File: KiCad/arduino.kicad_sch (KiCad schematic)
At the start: 15 parts, among them T3 ADS1115, T4 ADS1115

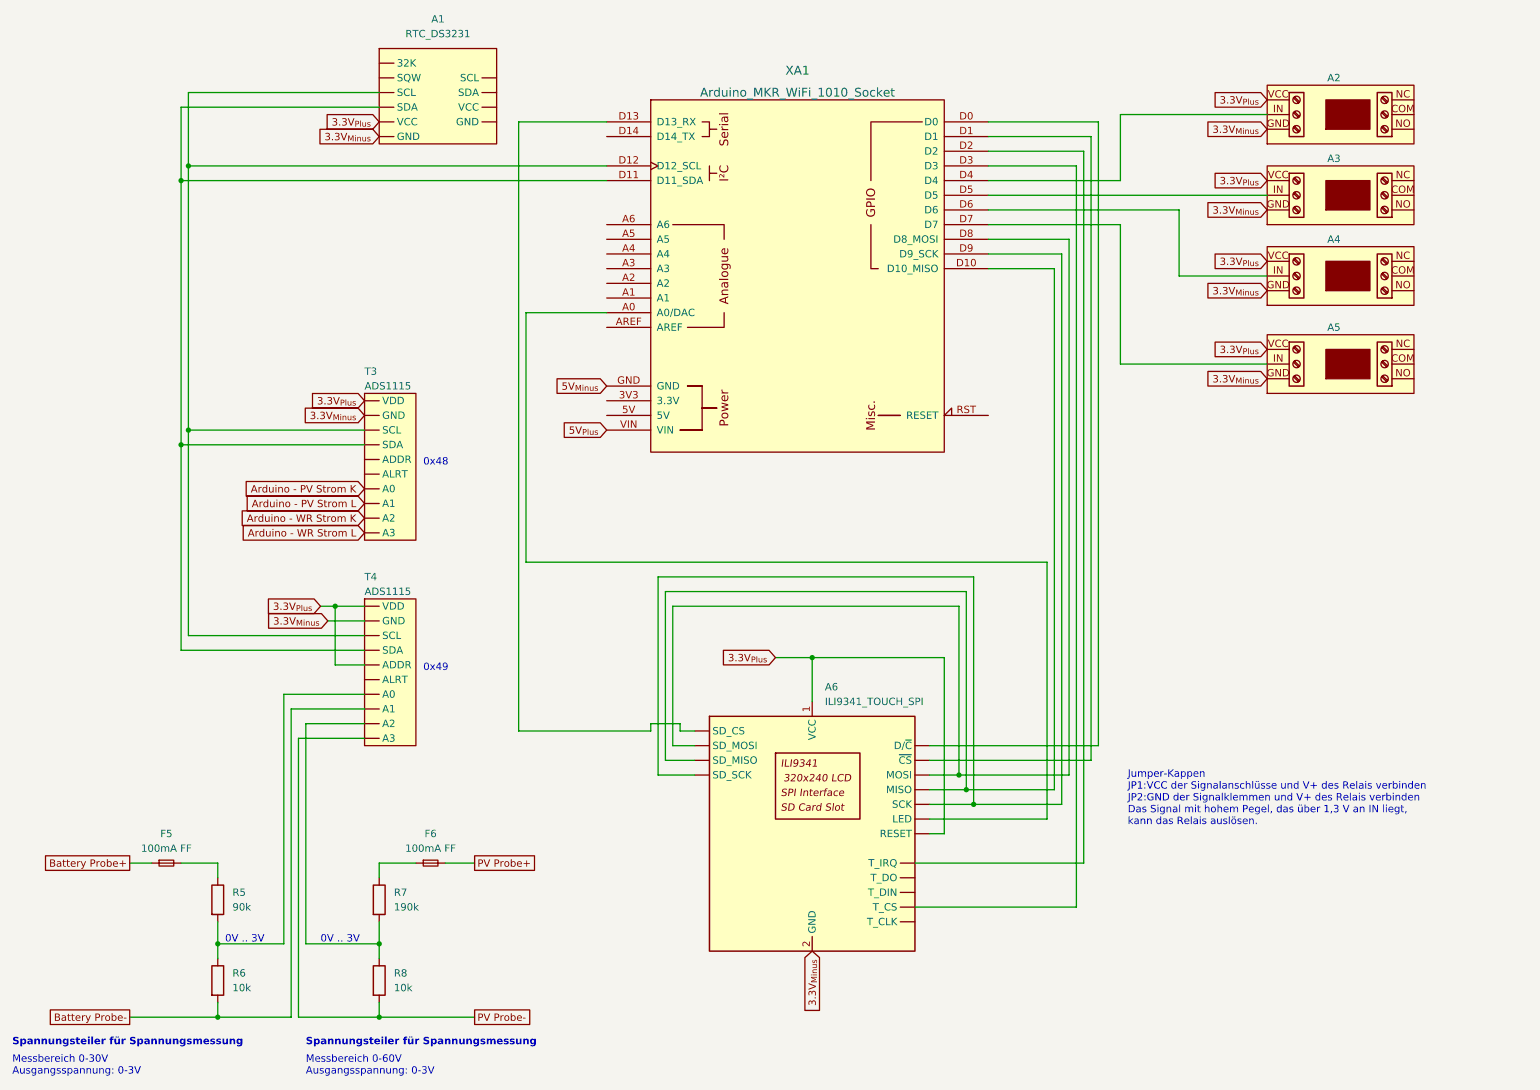
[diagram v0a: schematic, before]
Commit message: repository clean up | circuit diagram modified -> still have to add the wiring of the power supply in the circuit cabinet and the wiring of the UPS module
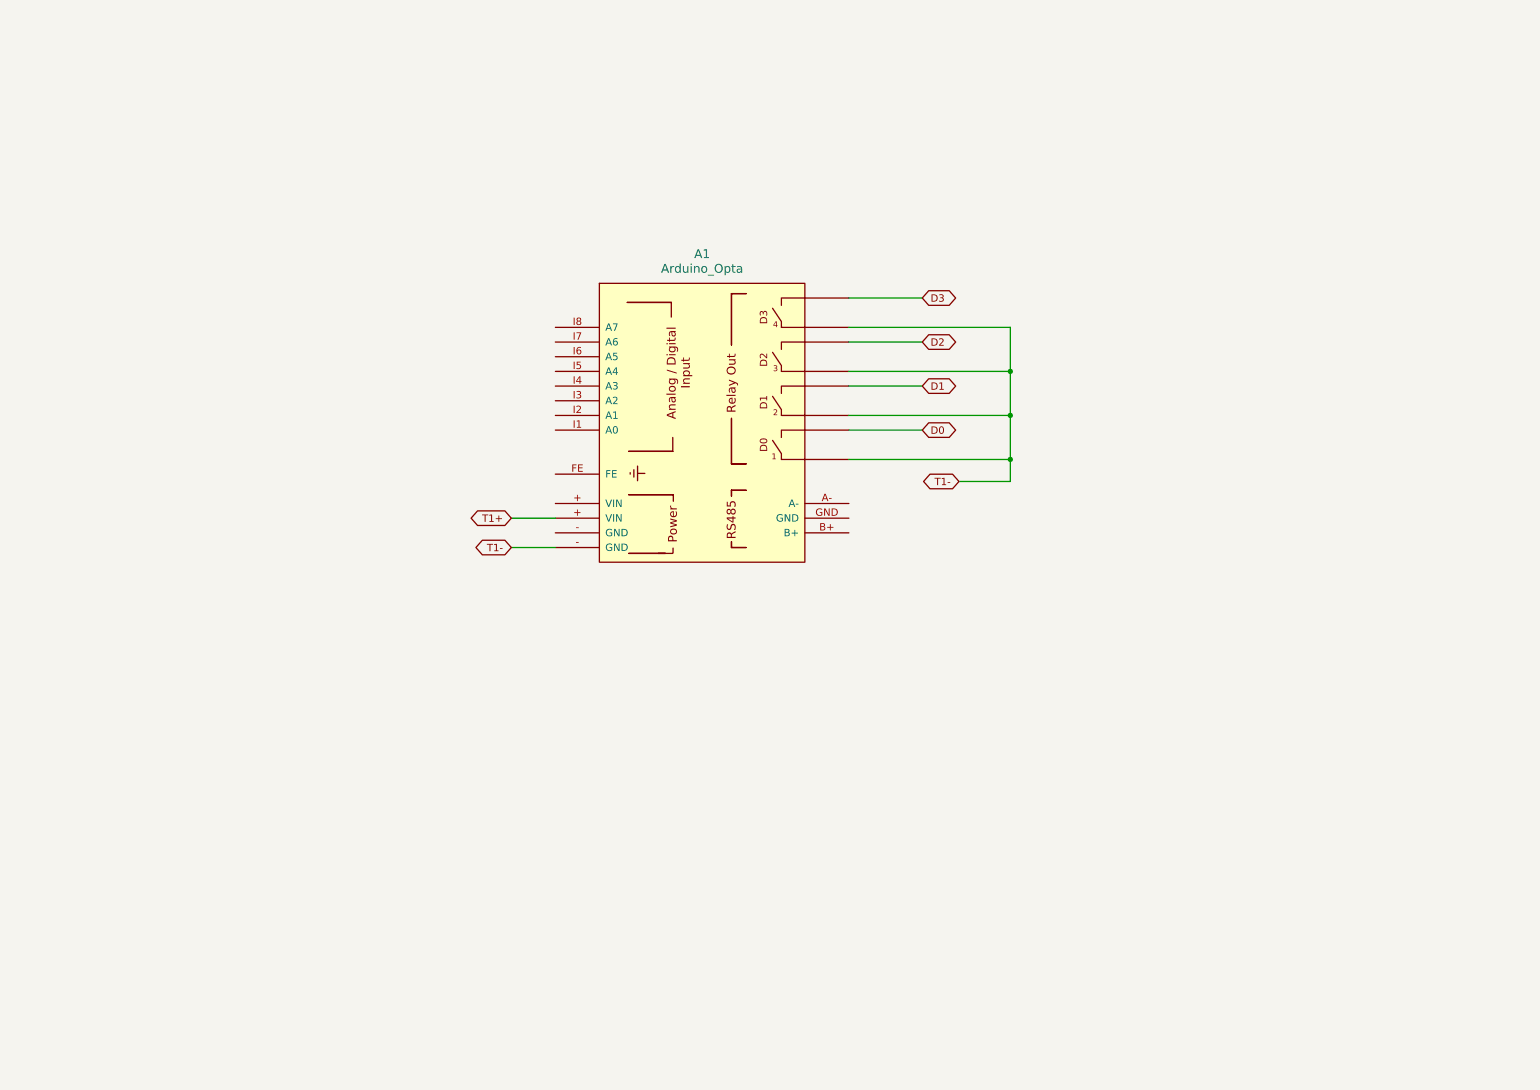
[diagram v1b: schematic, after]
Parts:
- removed A1: RTC_DS3231, symbol AlexanderTonnLib:RTC_DS3231
- removed A2, A3, A4, A5: Relay_Module, symbol AlexanderTonnLib:Relay_Module
- removed A6: ILI9341_TOUCH_SPI, symbol AlexanderTonnLib:ILI9341_TOUCH_SPI
- removed F5, F6: 100mA FF, symbol Device:Fuse_Small
- removed R5: 90k, symbol Device:R
- removed R6, R8: 10k, symbol Device:R
- removed R7: 190k, symbol Device:R
- removed T3, T4: ADS1115, symbol AlexanderTonnLib:ADS1115
- removed XA1: Arduino_MKR_WiFi_1010_Socket, Arduino_Library:Arduino_MKR_WiFi_1010_Socket, symbol Arduino Lib:Arduino_MKR_WiFi_1010_Socket
- added A1: Arduino_Opta, symbol Arduino:Arduino_Opta
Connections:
- new net D0: A1.
- new net D1: A1.
- new net D2: A1.
- new net D3: A1.
- new net T1+: A1.+ (VIN)
- new net T1-: A1., A1.- (GND)
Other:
- note removed: "0V .. 3V"
- note removed: "0x48"
- note removed: "0x49"
- note removed: "Jumper-Kappen JP1:VCC der Signalanschlüsse und V+ des Relais verbinden JP2:GND der Signalklemmen und V+ des Relais verbinden Das Signal mit hohem Pegel, das über 1,3 V an IN liegt, kann das Relais auslösen."
- note removed: "Messbereich 0-30V Ausgangsspannung: 0-3V"
- note removed: "Messbereich 0-60V Ausgangsspannung: 0-3V"
- note removed: "Spannungsteiler für Spannungsmessung"
- title: (none) -> Steuerstromkreis
